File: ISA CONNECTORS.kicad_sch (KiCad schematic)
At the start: 6 parts, among them J11001 ISA0, J11002 ISA0

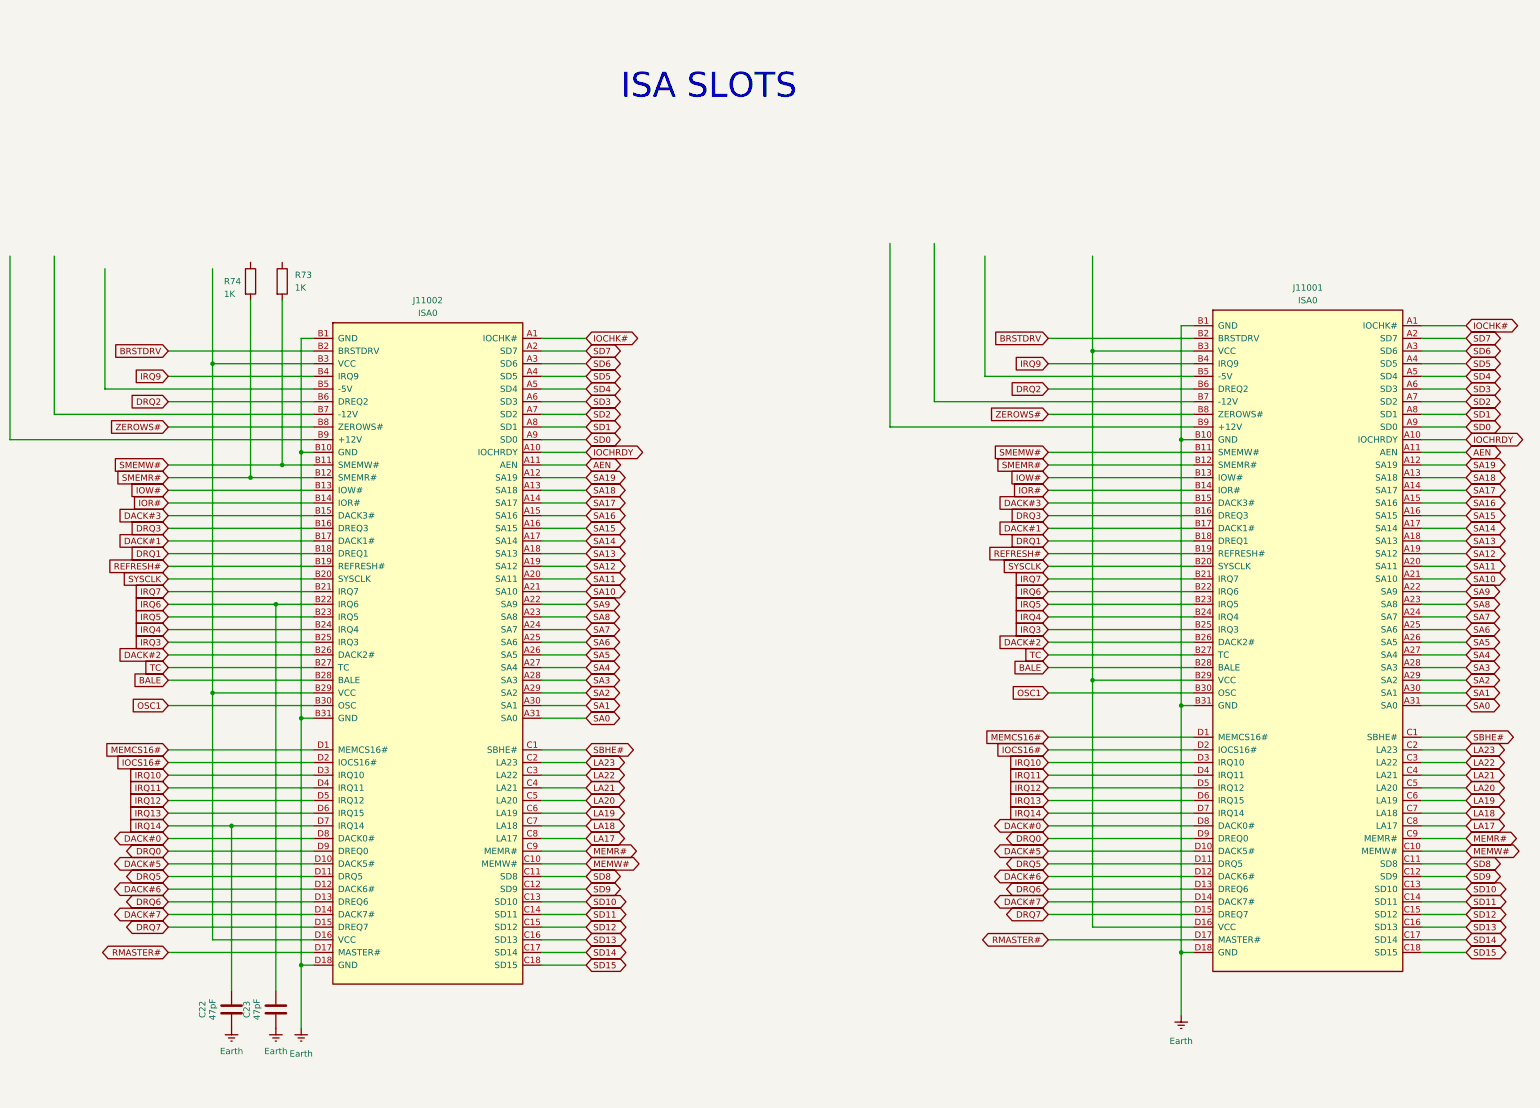
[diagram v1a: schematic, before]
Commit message: page 18 ISA, small fixes
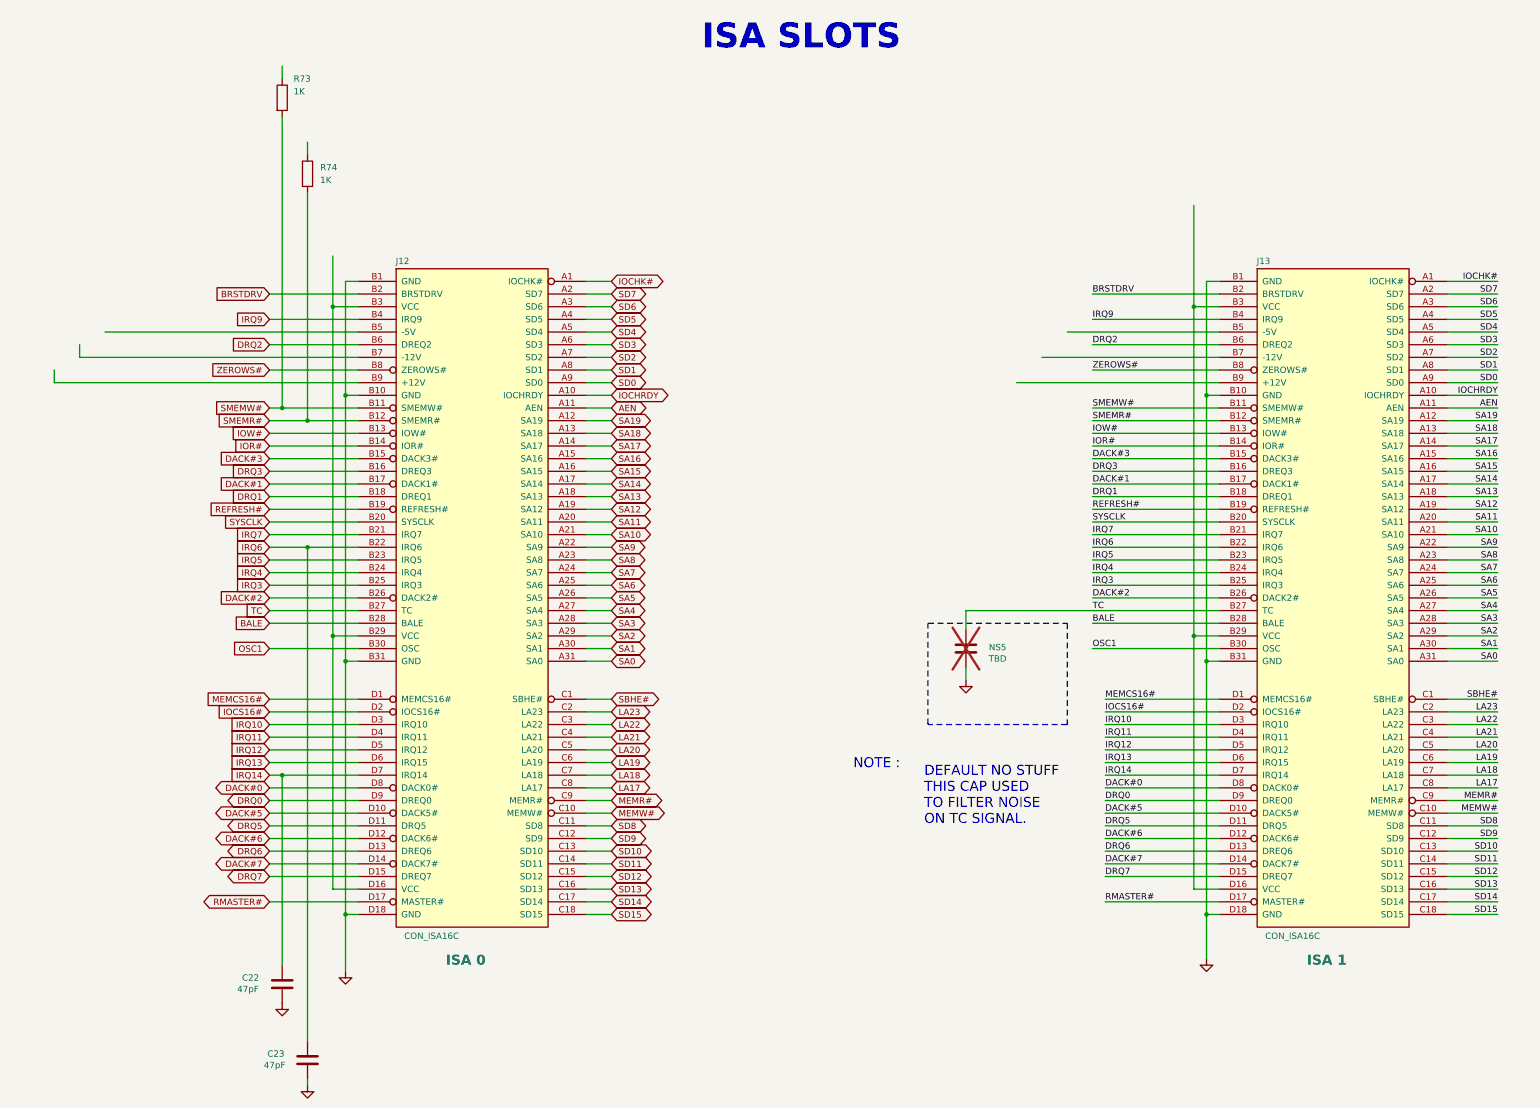
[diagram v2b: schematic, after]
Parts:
- removed J11001, J11002: ISA0, P2-3_ERA:ISA_GENERIC, symbol P2-3_era:ISA_GENERIC
- added J12: ISA 0, P2-3_ERA:ISA_GENERIC, symbol P2-3_era:ISA_Slot
- added J13: ISA 1, P2-3_ERA:ISA_GENERIC, symbol P2-3_era:ISA_Slot
- added NS5: TBD, Capacitor_SMD:C_0201_0603Metric, symbol Device:C
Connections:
- net AEN: now also J12.A11 (AEN), J13.A11 (AEN)
- net BALE: now also J12.B28 (BALE), J13.B28 (BALE)
- net BRSTDRV: now also J12.B2 (BRSTDRV), J13.B2 (BRSTDRV)
- net DACK#0: now also J12.D8 (DACK0#), J13.D8 (DACK0#)
- net DACK#1: now also J12.B17 (DACK1#), J13.B17 (DACK1#)
- net DACK#2: now also J12.B26 (DACK2#), J13.B26 (DACK2#)
- net DACK#3: now also J12.B15 (DACK3#), J13.B15 (DACK3#)
- net DACK#5: now also J12.D10 (DACK5#), J13.D10 (DACK5#)
- net DACK#6: now also J12.D12 (DACK6#), J13.D12 (DACK6#)
- net DACK#7: now also J12.D14 (DACK7#), J13.D14 (DACK7#)
- net DRQ0: now also J12.D9 (DREQ0), J13.D9 (DREQ0)
- net DRQ1: now also J12.B18 (DREQ1), J13.B18 (DREQ1)
- net DRQ2: now also J12.B6 (DREQ2), J13.B6 (DREQ2)
- net DRQ3: now also J12.B16 (DREQ3), J13.B16 (DREQ3)
- net DRQ5: now also J12.D11 (DRQ5), J13.D11 (DRQ5)
- net DRQ6: now also J12.D13 (DREQ6), J13.D13 (DREQ6)
- net DRQ7: now also J12.D15 (DREQ7), J13.D15 (DREQ7)
- net IOCHK#: now also J12.A1 (IOCHK#), J13.A1 (IOCHK#)
- net IOCHRDY: now also J12.A10 (IOCHRDY), J13.A10 (IOCHRDY)
- net IOCS16#: now also J12.D2 (IOCS16#), J13.D2 (IOCS16#)
- net IOR#: now also J12.B14 (IOR#), J13.B14 (IOR#)
- net IOW#: now also J12.B13 (IOW#), J13.B13 (IOW#)
- net IRQ10: now also J12.D3 (IRQ10), J13.D3 (IRQ10)
- net IRQ11: now also J12.D4 (IRQ11), J13.D4 (IRQ11)
- net IRQ12: now also J12.D5 (IRQ12), J13.D5 (IRQ12)
- net IRQ13: now also J12.D6 (IRQ15), J13.D6 (IRQ15)
- net IRQ14: now also J12.D7 (IRQ14), J13.D7 (IRQ14)
- net IRQ3: now also J12.B25 (IRQ3), J13.B25 (IRQ3)
- net IRQ4: now also J12.B24 (IRQ4), J13.B24 (IRQ4)
- net IRQ5: now also J12.B23 (IRQ5), J13.B23 (IRQ5)
- net IRQ6: now also J12.B22 (IRQ6), J13.B22 (IRQ6)
- net IRQ7: now also J12.B21 (IRQ7), J13.B21 (IRQ7)
- net IRQ9: now also J12.B4 (IRQ9), J13.B4 (IRQ9)
- net LA17: now also J12.C8 (LA17), J13.C8 (LA17)
- net LA18: now also J12.C7 (LA18), J13.C7 (LA18)
- net LA19: now also J12.C6 (LA19), J13.C6 (LA19)
- net LA20: now also J12.C5 (LA20), J13.C5 (LA20)
- net LA21: now also J12.C4 (LA21), J13.C4 (LA21)
- net LA22: now also J12.C3 (LA22), J13.C3 (LA22)
- net LA23: now also J12.C2 (LA23), J13.C2 (LA23)
- net MEMCS16#: now also J12.D1 (MEMCS16#), J13.D1 (MEMCS16#)
- net MEMR#: now also J12.C9 (MEMR#), J13.C9 (MEMR#)
- net MEMW#: now also J12.C10 (MEMW#), J13.C10 (MEMW#)
- net OSC1: now also J12.B30 (OSC), J13.B30 (OSC)
- net REFRESH#: now also J12.B19 (REFRESH#), J13.B19 (REFRESH#)
- net RMASTER#: now also J12.D17 (MASTER#), J13.D17 (MASTER#)
- net SA0: now also J12.A31 (SA0), J13.A31 (SA0)
- net SA1: now also J12.A30 (SA1), J13.A30 (SA1)
- net SA10: now also J12.A21 (SA10), J13.A21 (SA10)
- net SA11: now also J12.A20 (SA11), J13.A20 (SA11)
- net SA12: now also J12.A19 (SA12), J13.A19 (SA12)
- net SA13: now also J12.A18 (SA13), J13.A18 (SA13)
- net SA14: now also J12.A17 (SA14), J13.A17 (SA14)
- net SA15: now also J12.A16 (SA15), J13.A16 (SA15)
- net SA16: now also J12.A15 (SA16), J13.A15 (SA16)
- net SA17: now also J12.A14 (SA17), J13.A14 (SA17)
- net SA18: now also J12.A13 (SA18), J13.A13 (SA18)
- net SA19: now also J12.A12 (SA19), J13.A12 (SA19)
- net SA2: now also J12.A29 (SA2), J13.A29 (SA2)
- net SA3: now also J12.A28 (SA3), J13.A28 (SA3)
- net SA4: now also J12.A27 (SA4), J13.A27 (SA4)
- net SA5: now also J12.A26 (SA5), J13.A26 (SA5)
- net SA6: now also J12.A25 (SA6), J13.A25 (SA6)
- net SA7: now also J12.A24 (SA7), J13.A24 (SA7)
- net SA8: now also J12.A23 (SA8), J13.A23 (SA8)
- net SA9: now also J12.A22 (SA9), J13.A22 (SA9)
- net SBHE#: now also J12.C1 (SBHE#), J13.C1 (SBHE#)
- net SD0: now also J12.A9 (SD0), J13.A9 (SD0)
- net SD1: now also J12.A8 (SD1), J13.A8 (SD1)
- net SD10: now also J12.C13 (SD10), J13.C13 (SD10)
- net SD11: now also J12.C14 (SD11), J13.C14 (SD11)
- net SD12: now also J12.C15 (SD12), J13.C15 (SD12)
- net SD13: now also J12.C16 (SD13), J13.C16 (SD13)
- net SD14: now also J12.C17 (SD14), J13.C17 (SD14)
- net SD15: now also J12.C18 (SD15), J13.C18 (SD15)
- net SD2: now also J12.A7 (SD2), J13.A7 (SD2)
- net SD3: now also J12.A6 (SD3), J13.A6 (SD3)
- net SD4: now also J12.A5 (SD4), J13.A5 (SD4)
- net SD5: now also J12.A4 (SD5), J13.A4 (SD5)
- net SD6: now also J12.A3 (SD6), J13.A3 (SD6)
- net SD7: now also J12.A2 (SD7), J13.A2 (SD7)
- net SD8: now also J12.C11 (SD8), J13.C11 (SD8)
- net SD9: now also J12.C12 (SD9), J13.C12 (SD9)
- net SMEMR#: now also J12.B12 (SMEMR#), J13.B12 (SMEMR#)
- net SMEMW#: now also J12.B11 (SMEMW#), J13.B11 (SMEMW#)
- net SYSCLK: now also J12.B20 (SYSCLK), J13.B20 (SYSCLK)
- net TC: now also J12.B27 (TC), J13.B27 (TC), NS5.1
- net ZEROWS#: now also J12.B8 (ZEROWS#), J13.B8 (ZEROWS#)
- net Earth renamed GND
- net GND: now also J12.B1 (GND), J12.B10 (GND), J12.B31 (GND), J12.D18 (GND), J13.B1 (GND), J13.B10 (GND), J13.B31 (GND), J13.D18 (GND), NS5.2
- new net: J12.B29 (VCC), J12.B3 (VCC), J12.D16 (VCC)
- new net: J13.B29 (VCC), J13.B3 (VCC), J13.D16 (VCC)
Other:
- note added: "DEFAULT NO STUFF THIS CAP USED TO FILTER NOISE ON TC SIGNAL."
- note added: "NOTE :"
- title: (none) -> ISA SLOTS
- moved on the sheet: C22, C23, R73, R74
